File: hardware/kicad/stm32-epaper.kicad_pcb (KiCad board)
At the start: 4 copper layers, 97.4 x 60 mm, 152 parts, among them J1 USB_C_Receptacle_USB2.0_16P, J101 TC2050-IDC-NL, J102 UART (TX RX GND), J2 BATT (1S LiPo), J201 microSD, J301 IT8951 HAT, J302 Electrodes L, J303 Electrodes R, SW101 BOOT, SW301 PEC11R-4220F-S0024, SW302 POWER, U1 BQ24073RGT, U101 STM32F469IIT6, U2 TPS63802DLA, U201 IS42S16400J-6TLI, U202 W25Q128JVSIQ, U3 TPS61023DRL, U301 CAP1188-1-CP-TR, U302 TPD4E05U06DQAR, U4 TPS22965DSG, U5 USBLC6-2SC6, U6 TPS63900DSK, U7 MCP1700T-3002E/TT, Y101 8MHz CL8pF, Y102 32.768kHz CL6pF

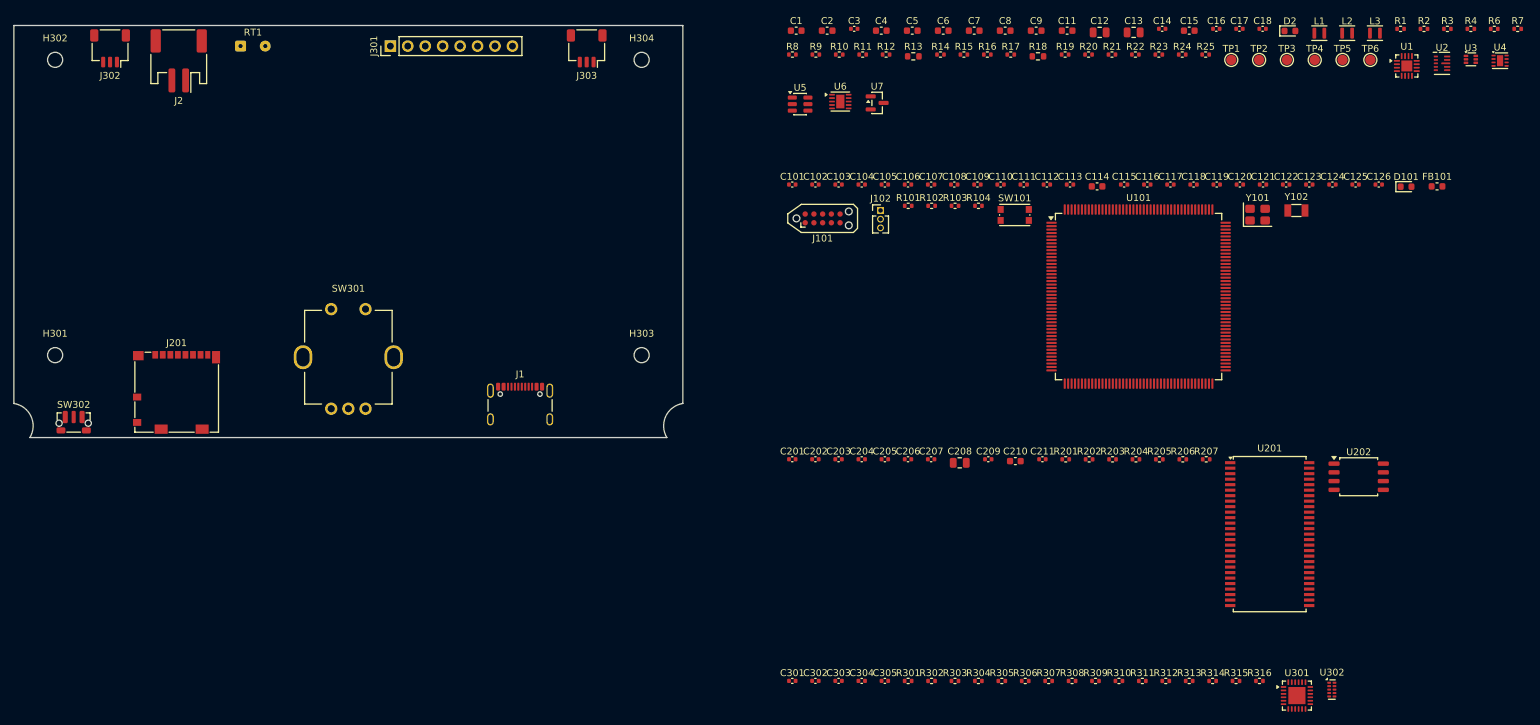
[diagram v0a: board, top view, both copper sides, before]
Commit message: Main PCB placement, layout rules, clock terminations, offline freerouting
- place_main_pcb.py: hand floorplan for the ICs plus a greedy placer
  (parts next to what they connect to, decoupling at their IC's power
  pins, clock series resistors at their MCU pins), inner planes
  In1 = GND / In2 = +3V3. CAP1188 moved top-middle between J302/J303.
- Net classes (Power, Rail3V3, Touch, Clock) set by gen_main_pcb.py and
  exported to the router; stm32-epaper.kicad_dru adds length/skew limits
  for the SDRAM/SDIO/QSPI buses, USB pair, crystals and touch lines,
  checked by KiCad DRC after routing.
- Schematic: 22/33R source series resistors R208-R210 on the SDRAM,
  microSD and QSPI clocks; check_schematic.py verifies they bridge the
  right nets.
- route_main_pcb.py: Specctra DSN/SES round trip for headless freerouting.
- .mcp.json: freerouting MCP server switched to the local jar (offline, no
  API key).
- docs/DS_stm32f469ae.pdf added; LSE margin checked (needs high-drive mode).
- Enclosure: fit-check print export (chin section + knob) and checklist.

Co-Authored-By: Claude Opus 5.5 <noreply@anthropic.com>
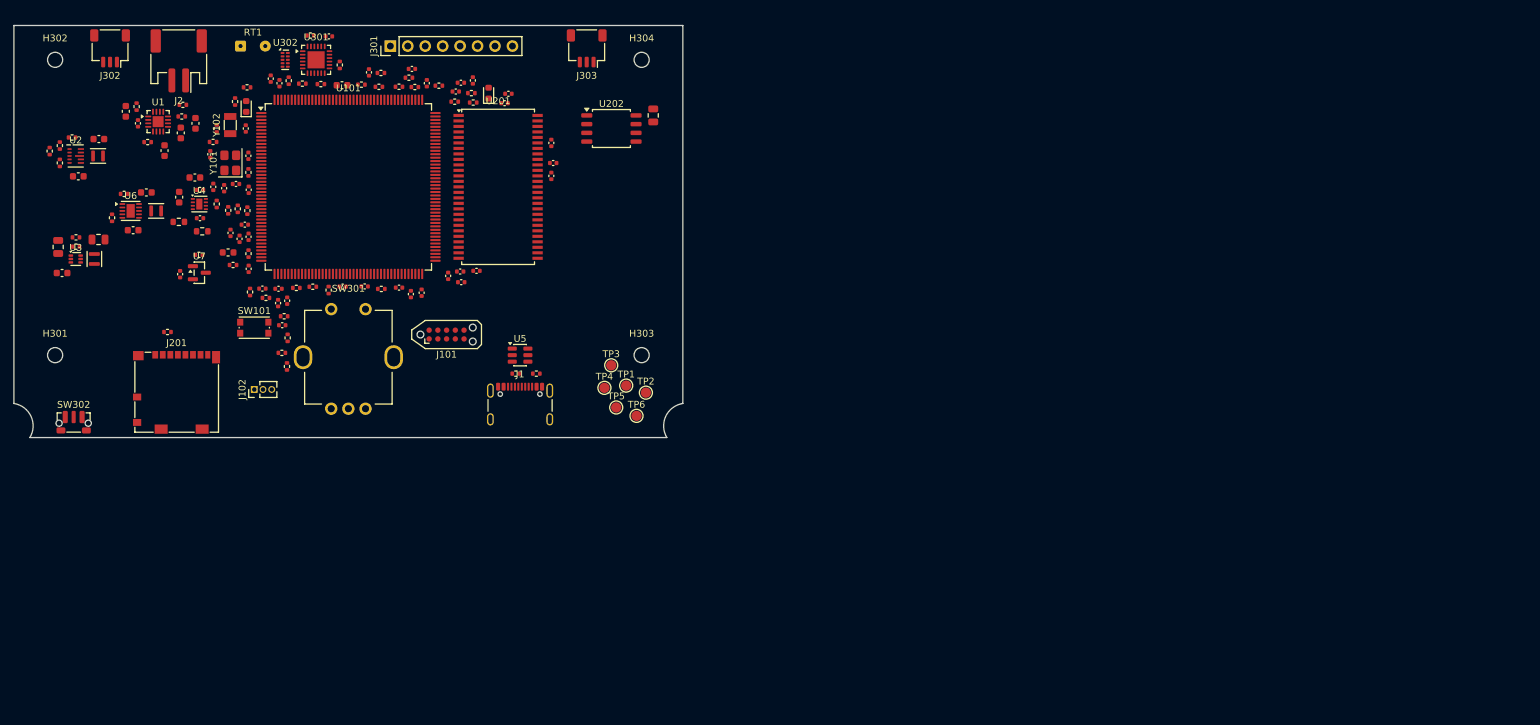
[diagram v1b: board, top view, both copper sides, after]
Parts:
- added R208: 22R, Resistor_SMD:R_0402_1005Metric, F.Cu at (166.9, 111.2)
- added R209: 33R, Resistor_SMD:R_0402_1005Metric, F.Cu at (156.1, 108.9)
- added R210: 22R, Resistor_SMD:R_0402_1005Metric, F.Cu at (129.5, 126.0)
- moved R7 213.2 mm to (106.7, 120.0), turned to 90 degrees
- moved R6 207.7 mm to (108.5, 116.3)
- moved U3 205.2 mm to (109.0, 134.0)
- moved U2 199.4 mm to (109.0, 119.0)
- moved R3 191.2 mm to (117.9, 111.8), turned to 90 degrees
- moved U4 190.5 mm to (127.0, 126.0)
- moved L2 185.4 mm to (111.7, 134.0), turned to 90 degrees
- moved U1 182.0 mm to (121.0, 114.0)
- moved L3 179.3 mm to (120.7, 127.0)
- moved L1 178.7 mm to (112.2, 119.0)
- moved R4 178.4 mm to (133.9, 109.0)
- moved U302 177.9 mm to (139.5, 105.0)
- moved FB101 176.3 mm to (131.2, 133.1)
- moved U301 170.2 mm to (144.0, 105.0)
- moved C15 167.9 mm to (107.0, 136.0)
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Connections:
- J201 pad 5: SDIO_CK -> SDCARD_CLK
- U201 pad 38: FMC_SDCLK -> SDRAM_CLK
- U202 pad 6: QUADSPI_CLK -> QSPI_FLASH_CLK
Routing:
- added copper zone on In2.Cu, net +3V3
- added copper zone on In1.Cu, net GND

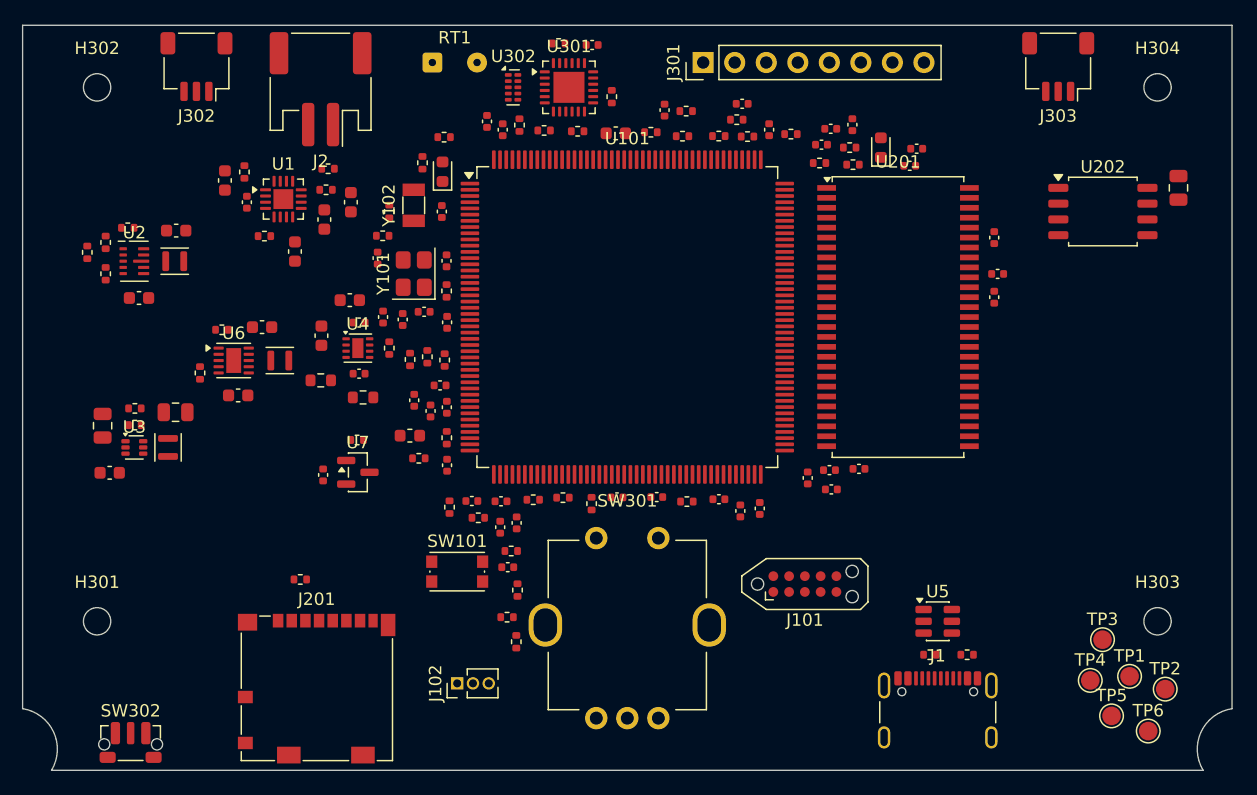
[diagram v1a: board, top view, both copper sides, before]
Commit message: Routing attempt 1 (baseline): split In2 planes, smd_smd DSN fix, loop tooling
81 unconnected / 15 nets (mostly plane nets), 0 clearance errors; see
hardware/kicad/routing-log.md.

Co-Authored-By: Claude Opus 5.5 <noreply@anthropic.com>
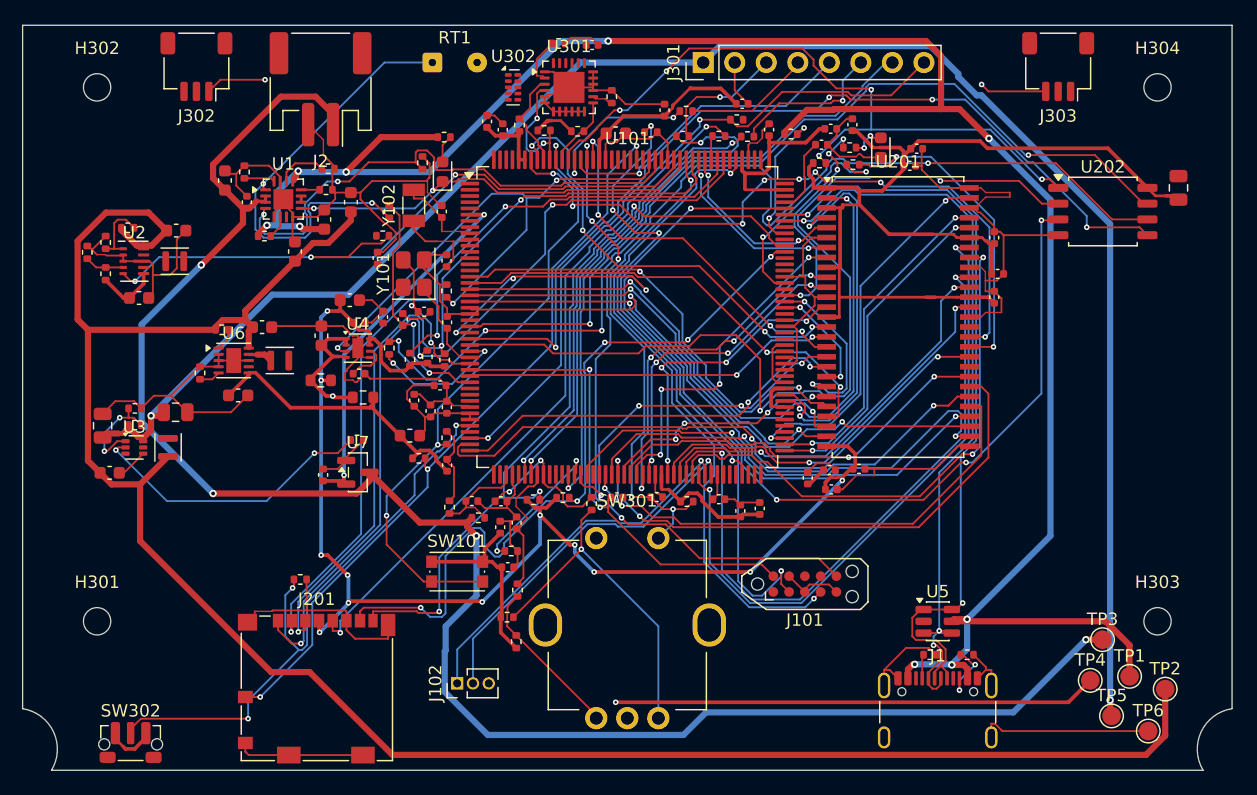
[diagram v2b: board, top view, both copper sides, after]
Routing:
- net GND: track 0.00 -> 332.9 mm
- net 3V3_PERIPH: track 0.00 -> 188.1 mm, vias 0 -> 12
- net VBUS: track 0.00 -> 173.2 mm, vias 0 -> 9
- net VSYS: track 0.00 -> 167.9 mm
- net +BATT: track 0.00 -> 145.6 mm, vias 0 -> 4
- net +5V: track 0.00 -> 142.6 mm, vias 0 -> 2
- net 3V3_AON: track 0.00 -> 98.6 mm
- net QUADSPI_BK1_IO2: track 0.00 -> 84.1 mm, vias 0 -> 6
- net QSPI_FLASH_CLK: track 0.00 -> 83.0 mm, vias 0 -> 4
- net QUADSPI_BK1_IO1: track 0.00 -> 76.4 mm, vias 0 -> 2
- net QUADSPI_BK1_IO0: track 0.00 -> 73.0 mm, vias 0 -> 4
- net SDIO_D2: track 0.00 -> 70.8 mm, vias 0 -> 3
- net QUADSPI_BK1_IO3: track 0.00 -> 69.8 mm, vias 0 -> 2
- net SDIO_D3: track 0.00 -> 68.6 mm, vias 0 -> 3
- net SDIO_CMD: track 0.00 -> 67.1 mm, vias 0 -> 3
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- added copper zone on In2.Cu, net 3V3_AON
- added copper zone on In2.Cu, net 3V3_PERIPH

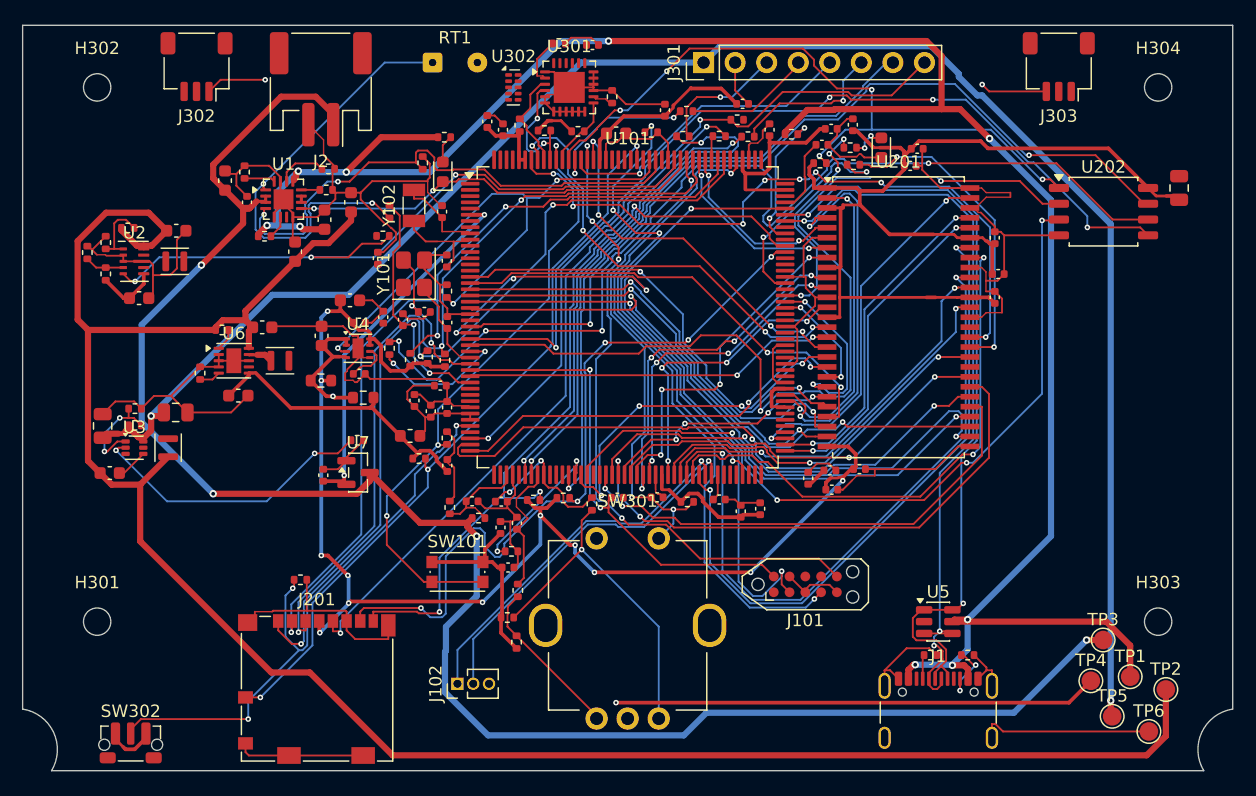
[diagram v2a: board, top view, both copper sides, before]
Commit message: Routing attempt 2: locked plane vias -> 43 unconnected (from 81)
Pre-router needs hole-to-hole spacing between same-net vias and
class-aware clearances (12 via DRC errors); placement optimiser for the
MCU rotation / memory positions added for the next attempt.

Co-Authored-By: Claude Opus 5.5 <noreply@anthropic.com>
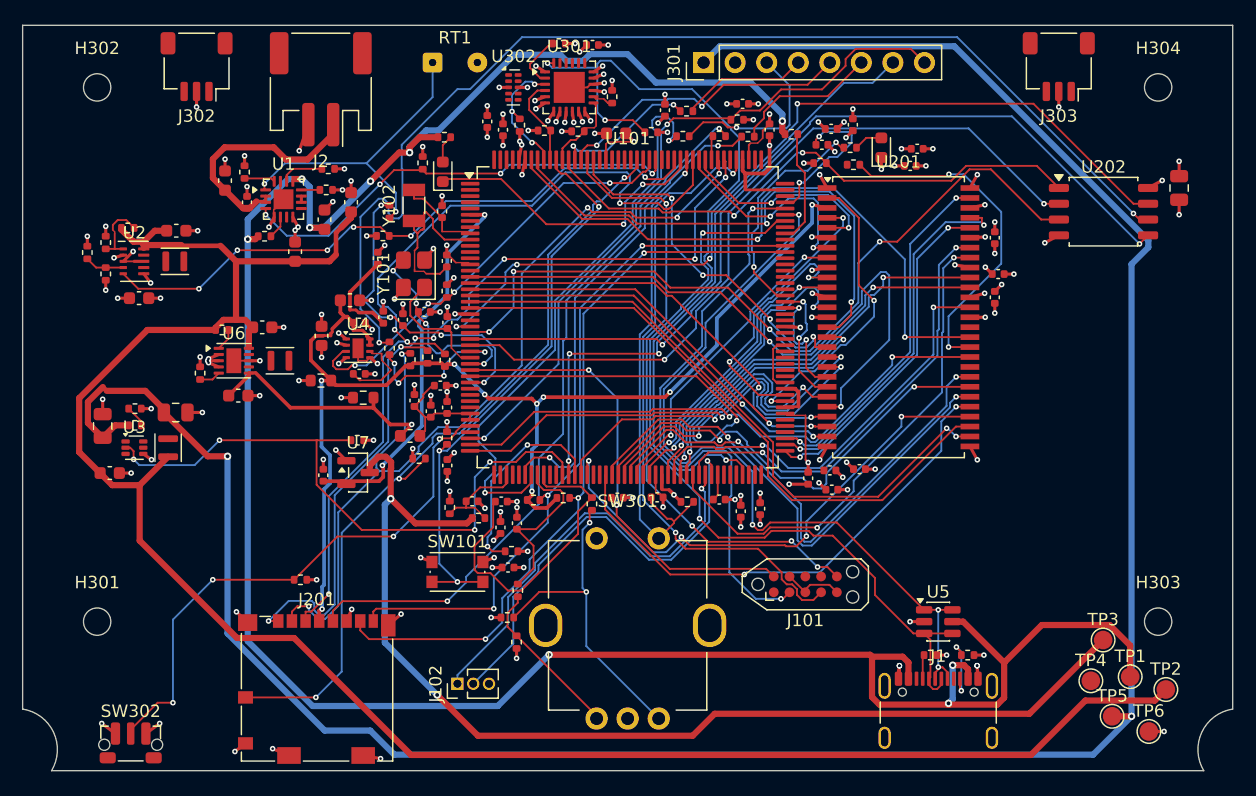
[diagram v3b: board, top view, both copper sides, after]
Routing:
- net GND: track 332.9 -> 155.4 mm, vias 0 -> 133
- net 3V3_PERIPH: track 188.1 -> 112.7 mm, vias 12 -> 26
- net +5V: track 142.6 -> 195.7 mm
- net +3V3: track 55.6 -> 8.64 mm, vias 2 -> 10
- net +BATT: track 145.6 -> 108.8 mm, vias 4 -> 2
- net 3V3_AON: track 98.6 -> 67.2 mm, vias 0 -> 28
- net EPD_5V_EN: track 23.5 -> 51.2 mm, vias 2 -> 4
- net CAP_RESET: track 38.5 -> 64.9 mm, vias 4 -> 3
- net VBUS: track 173.2 -> 199.5 mm
- net FMC_D10: track 53.8 -> 32.4 mm
- net QUADSPI_BK1_IO2: track 84.1 -> 63.4 mm, vias 6 -> 4
- net FMC_SDCLK: track 18.0 -> 0.00 mm, vias 2 -> 0
- net FMC_D12: track 52.1 -> 35.5 mm
- net FMC_A0: track 37.2 -> 53.1 mm
- net FMC_SDNWE: track 30.0 -> 44.6 mm
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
